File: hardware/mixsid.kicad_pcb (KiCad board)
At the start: 2 copper layers, 50.8 x 55.9 mm, 63 parts, among them P1 INPUT, P2 CONTROL, P4 SOCKET LEFT, P5 OUTPUT, P6 SOCKET RIGHT, Q1 BC547, Q2 BC547, U1 GAL16V8, U2 SID2, U3 7812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

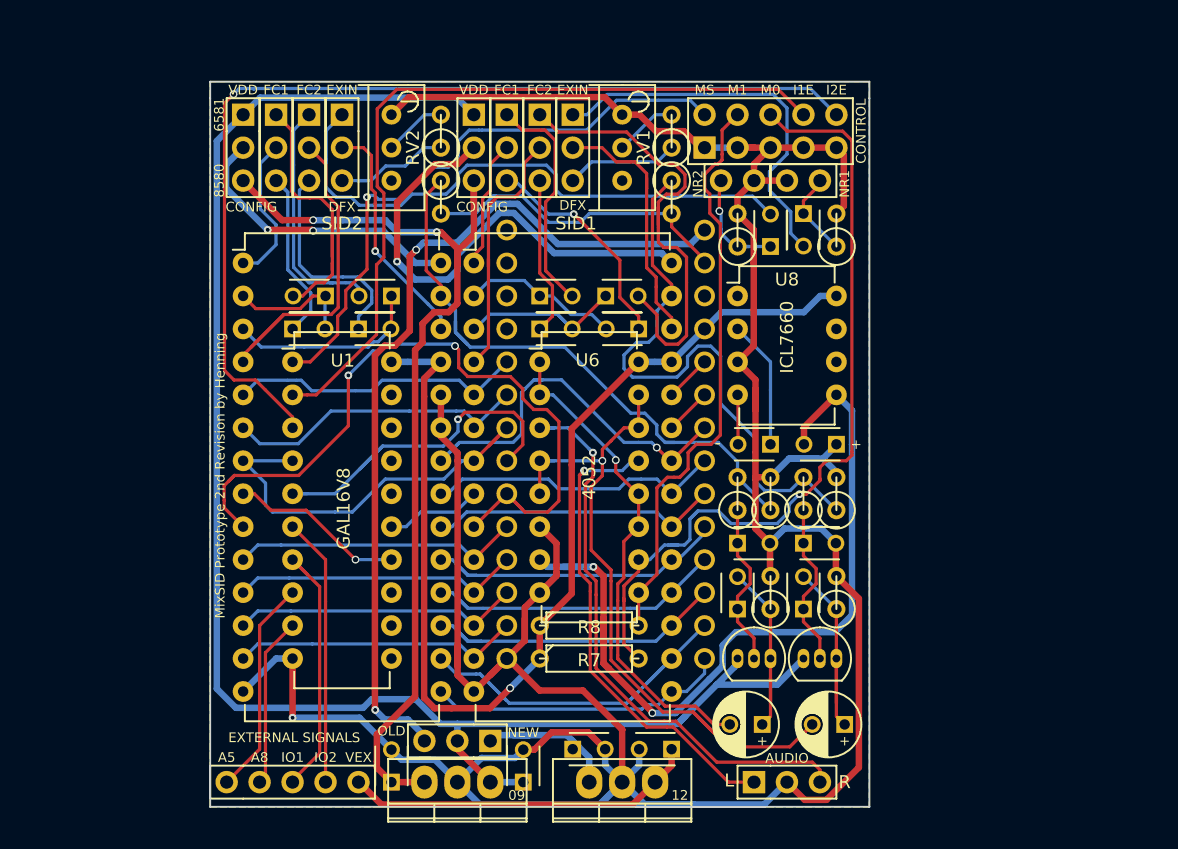
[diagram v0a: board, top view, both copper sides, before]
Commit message: Hardware: Added voltage dividers for optional volume adjustments
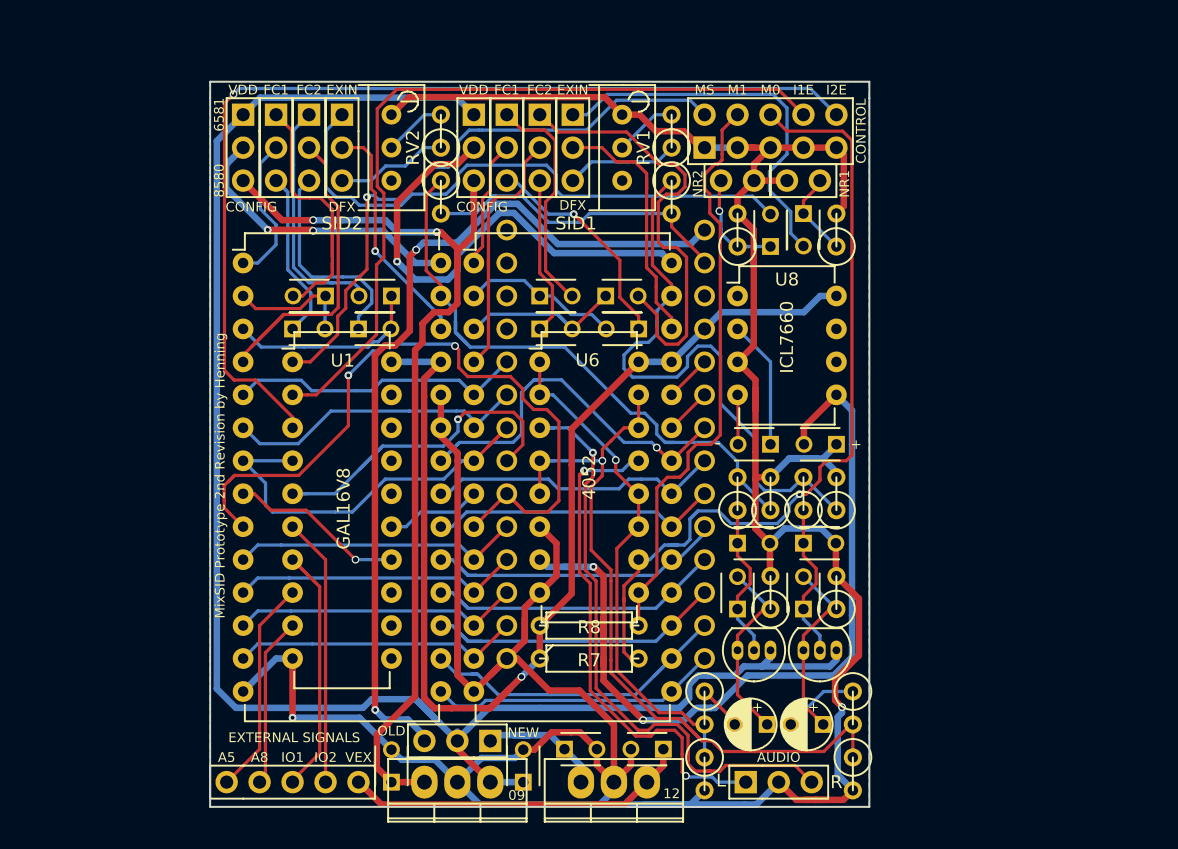
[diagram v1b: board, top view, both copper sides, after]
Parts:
- added R15: 0, Discret:R1, F.Cu at (166.4, 115.6)
- added R16: 0, Discret:R1, F.Cu at (166.4, 120.7)
- added R17: 0, Discret:R1, F.Cu at (177.8, 115.6)
- added R18: 0, Discret:R1, F.Cu at (177.8, 120.7)
- C19, C22: footprint Capacitors_ThroughHole:C_Radial_D5_L6_P2.5 -> Pinheaders:C_Radial_D5_L6_P2.5
- moved Q1 2.62 mm to (171.4, 111.1), turned to 180 degrees
- moved Q2 2.62 mm to (176.5, 111.1), turned to 180 degrees
- moved C22 1.65 mm to (175.5, 116.8)
- moved C5 0.64 mm to (163.2, 118.7)
- moved C6 0.64 mm to (155.6, 118.7)
- moved P5 0.64 mm to (169.5, 121.3)
- moved U3 0.64 mm to (159.4, 121.3)
- moved C19 0.38 mm to (171.2, 116.8)
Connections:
- C19 pad 2: /LEFT -> Net-(C19-Pad2)
- C22 pad 2: /RIGHT -> Net-(C22-Pad2)
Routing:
- net /D1: track 32.7 -> 25.9 mm
- net Net-(C22-Pad2): track 0.00 -> 5.84 mm
- net /+12V: track 124.5 -> 129.6 mm
- net /RIGHT: track 54.9 -> 59.9 mm
- net Net-(C19-Pad2): track 0.00 -> 3.97 mm
- net /LEFT_OUT: track 37.1 -> 40.8 mm, vias 1 -> 2
- net /VEE: track 63.4 -> 66.3 mm
- net /RIGHT_OUT: track 46.2 -> 48.7 mm
- net VCC: track 84.4 -> 86.6 mm
- net Net-(C21-Pad2): track 16.2 -> 14.4 mm
- net GND: track 279.6 -> 278.2 mm, vias 1 -> 2
- net (no net): track 1.36 -> 0.00 mm
- net /LEFT: track 38.1 -> 39.3 mm
- net /PWR: track 12.6 -> 11.6 mm
- net /VEXT: track 27.4 -> 28.2 mm
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
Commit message: Hardware: Changed 7660 caps to small electrolytics, improved silkscreen
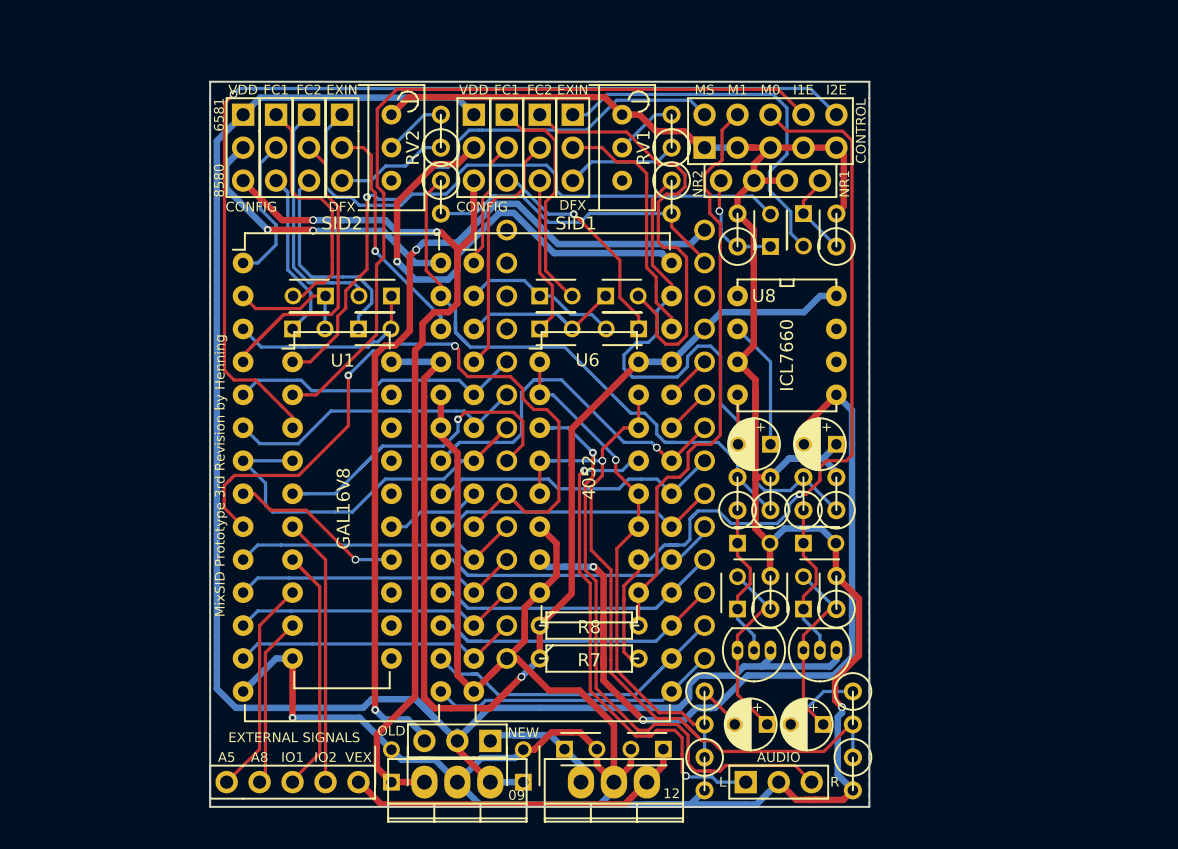
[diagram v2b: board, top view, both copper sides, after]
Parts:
- C17, C18: footprint Capacitors_ThroughHole:C_Disc_D3_P2.5 -> Pinheaders:C_Radial_D5_L6_P2.5
- R16, R18: value 0 -> ∞
- U8: footprint Housings_DIP:DIP-8_W7.62mm -> Pinheaders:DIP-8_W7.62mm
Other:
- board text added: "MixSID Prototype 3rd Revision by Henning"
- board text removed: "+"
- board text removed: "-"
- board text removed: "MixSID Prototype 2nd Revision by Henning"

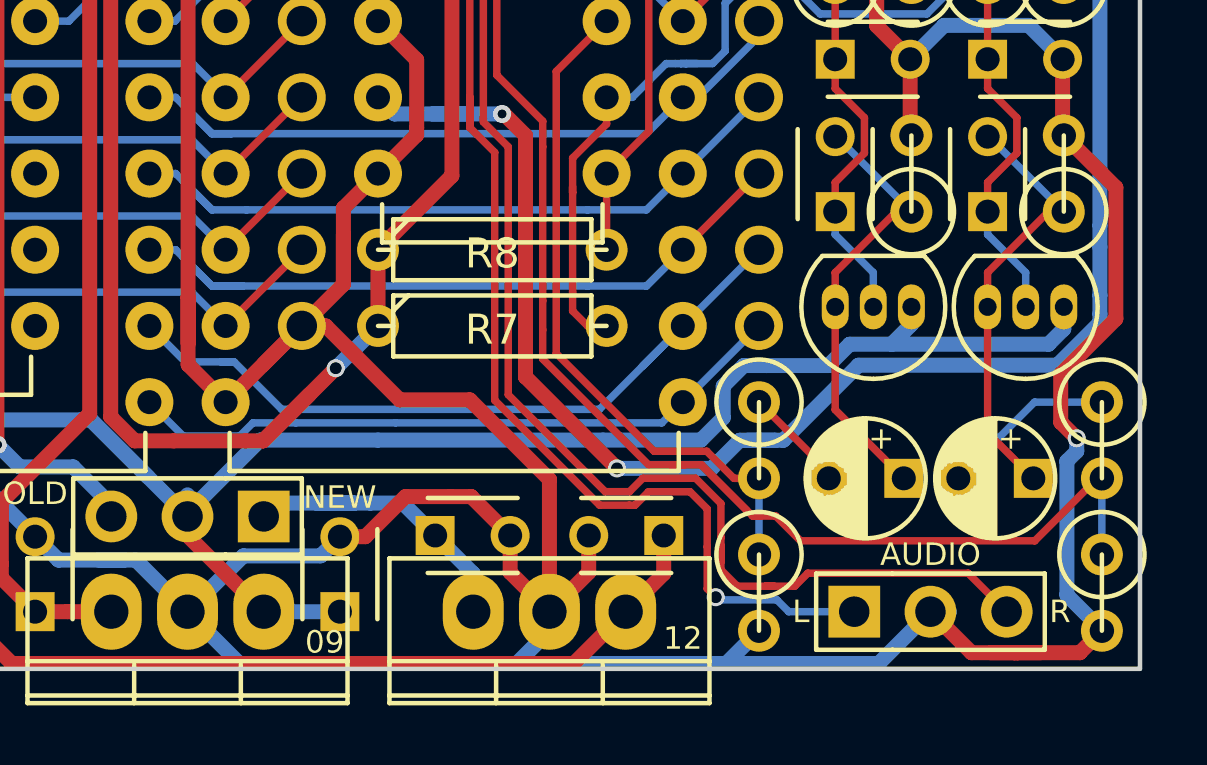
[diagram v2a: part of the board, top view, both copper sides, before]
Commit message: Hardware: Improved routing, scaled caps 3d models to size, improved 3d view
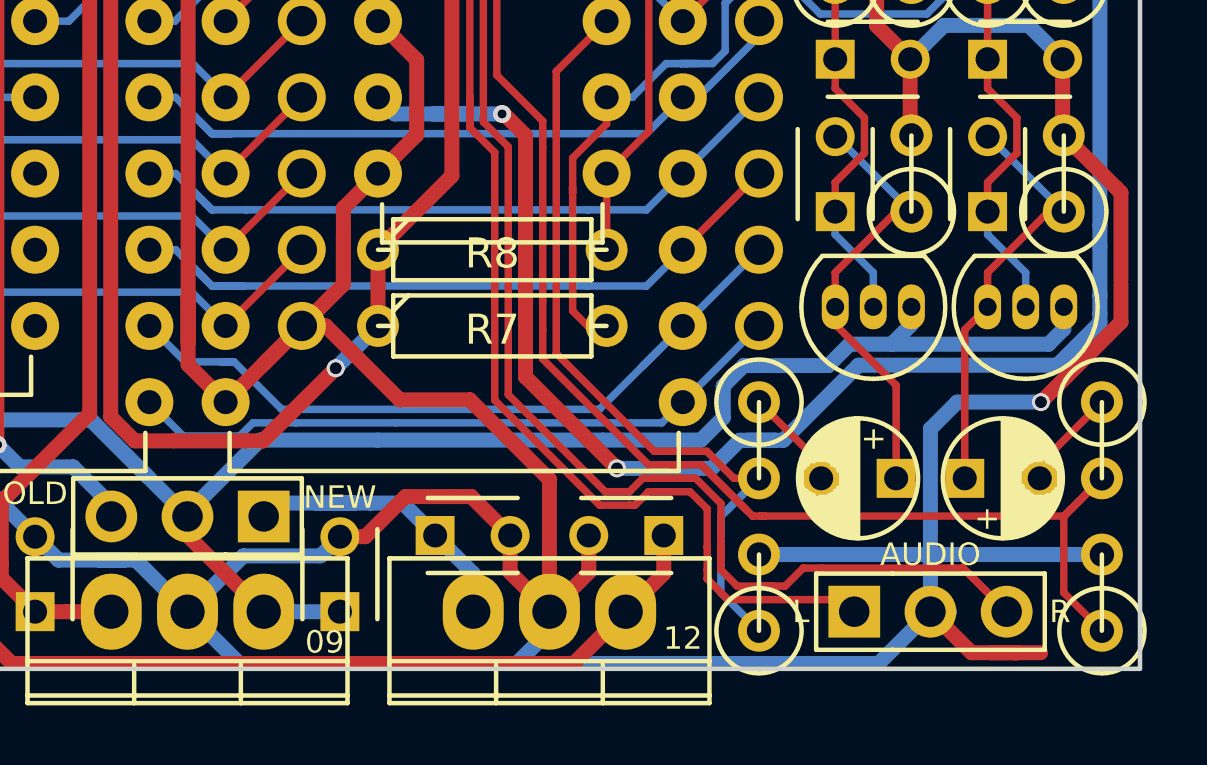
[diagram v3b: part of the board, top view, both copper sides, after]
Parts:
- moved C22 2.29 mm to (173.2, 116.8), turned to 0 degrees
- moved C19 0.25 mm to (170.9, 116.8)
- turned R16 to 90 degrees
- turned R18 to 90 degrees
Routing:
- net GND: track 278.2 -> 286.9 mm
- net /LEFT: track 39.3 -> 44.4 mm
- net /RIGHT: track 59.9 -> 63.1 mm
- net Net-(C22-Pad2): track 5.84 -> 3.40 mm
- net /RIGHT_OUT: track 48.7 -> 50.9 mm
- net /+12V: track 129.6 -> 128.9 mm
- net Net-(C19-Pad2): track 3.97 -> 3.40 mm
- net /LEFT_OUT: track 40.8 -> 40.6 mm, vias 2 -> 1

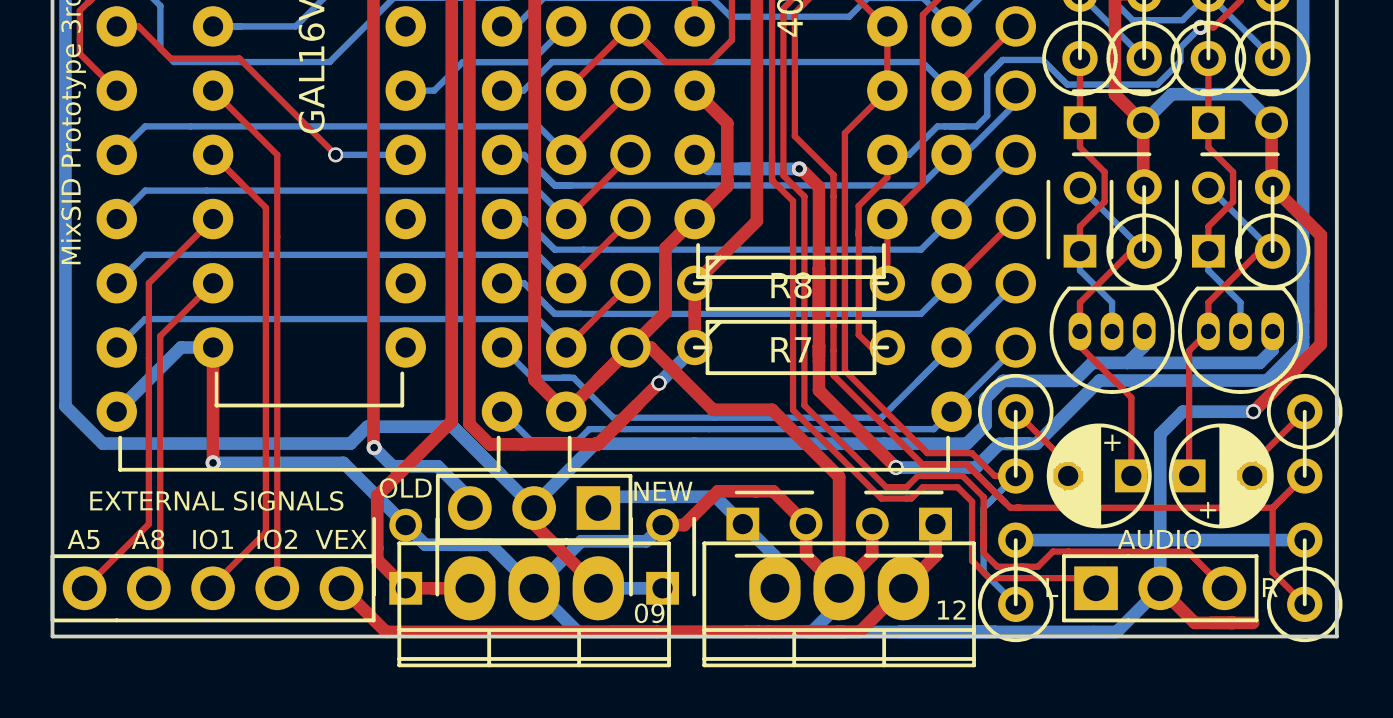
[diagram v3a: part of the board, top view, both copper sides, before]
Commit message: Hardware: Moved bottom connectors slightly up to save some more space
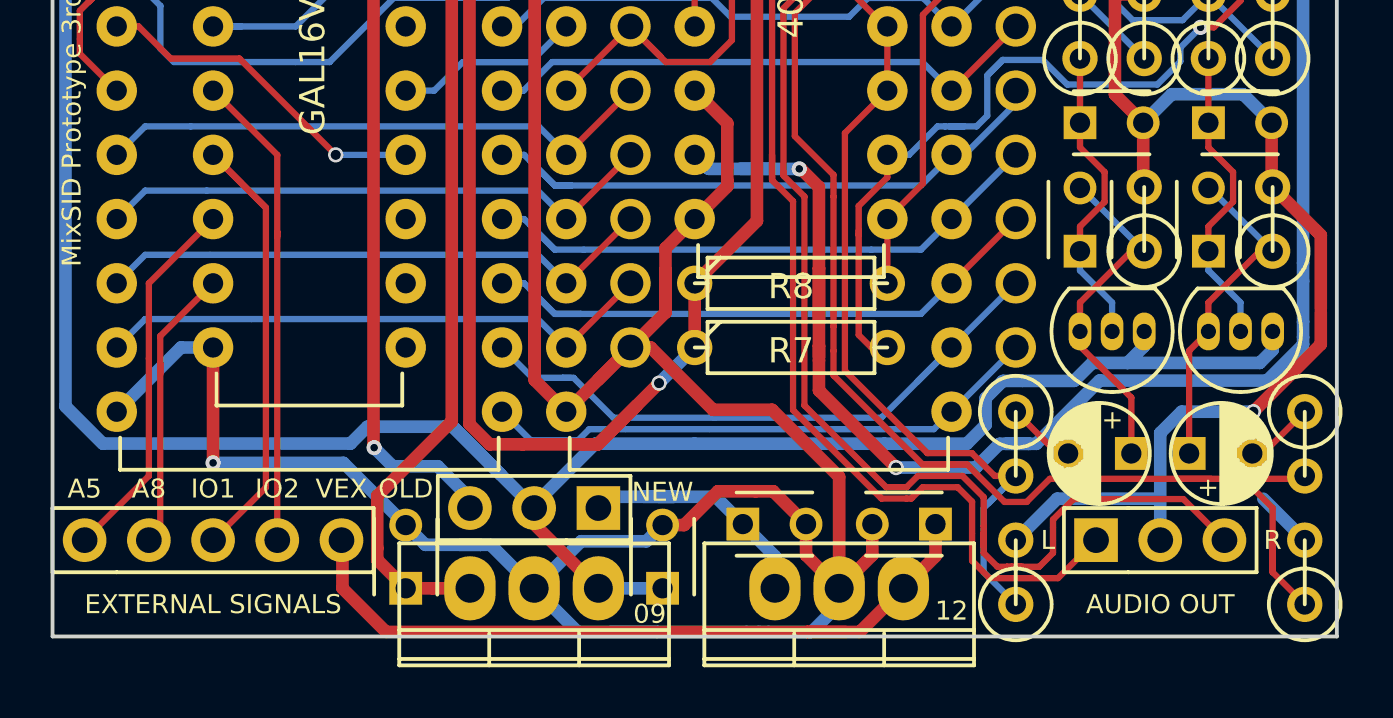
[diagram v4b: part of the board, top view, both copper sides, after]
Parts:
- moved P1 1.91 mm to (129.5, 119.4)
- moved P5 1.91 mm to (169.5, 119.4)
- moved C19 0.89 mm to (170.9, 116.0)
- moved C22 0.89 mm to (173.2, 116.0)
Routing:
- net GND: track 286.9 -> 251.2 mm
- net /A5: track 16.7 -> 14.8 mm
- net /VEXT: track 28.2 -> 30.1 mm
- net /~IO2: track 20.7 -> 19.0 mm
- net /A8: track 13.1 -> 11.7 mm
- net /~IO1: track 20.5 -> 21.5 mm
- net Net-(C21-Pad2): track 14.1 -> 13.2 mm
- net Net-(C22-Pad2): track 3.40 -> 2.76 mm
- net Net-(C19-Pad2): track 3.40 -> 2.76 mm
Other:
- board text added: "AUDIO OUT"
- board text removed: "AUDIO"
